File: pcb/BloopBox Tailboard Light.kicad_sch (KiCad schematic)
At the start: 18 parts, among them J1 USB_C_Receptacle_Power, J2 Barrel_Jack, J3 Mainboard, SW1 Button1, SW2 Button2, U1 HT7533-1

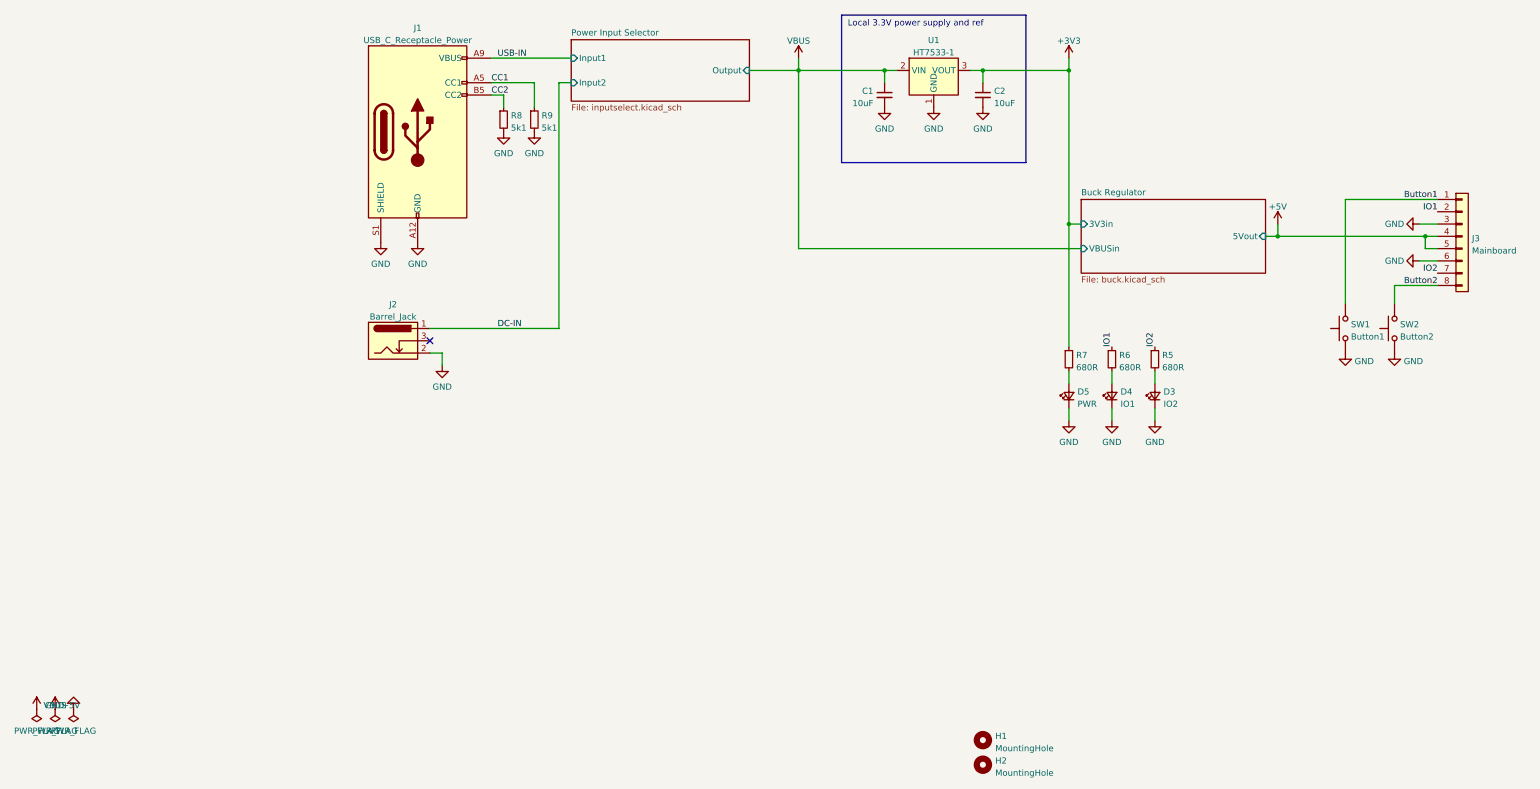
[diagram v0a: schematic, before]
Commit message: feat: remove active circuitry from schematics
Removing all active circuitry from the light-version of the Tailboard
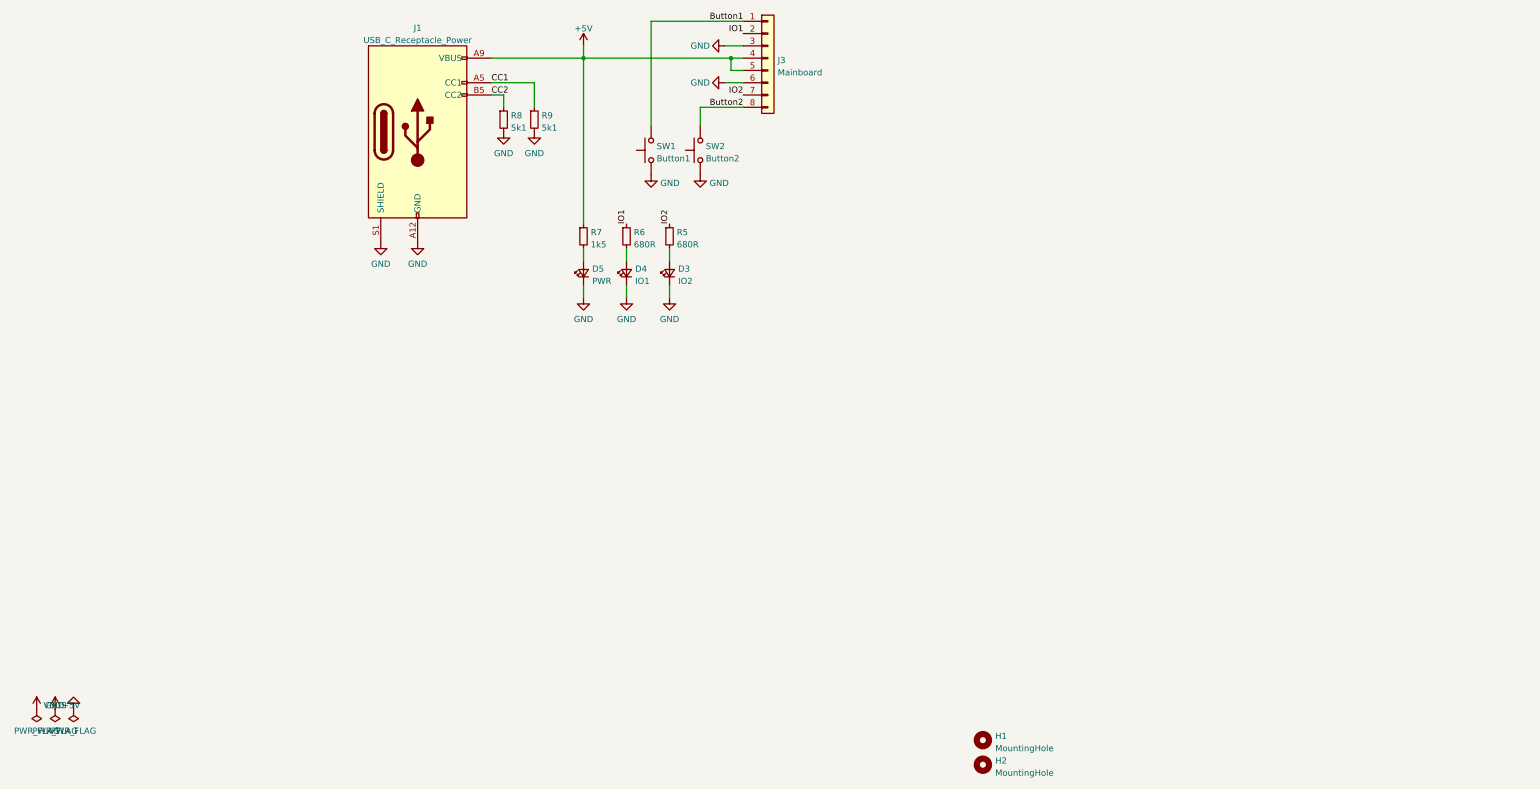
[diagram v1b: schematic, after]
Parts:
- removed C1: 10uF, Capacitor_SMD:C_0805_2012Metric, symbol Device:C_Small
- removed C2: 10uF, Capacitor_SMD:C_0402_1005Metric, symbol Device:C_Small
- removed J2: Barrel_Jack, Connector_BarrelJack:BarrelJack_Horizontal, symbol Connector:Barrel_Jack_Switch
- removed U1: HT7533-1, Package_TO_SOT_SMD:SOT-89-3, symbol Regulator_Linear:HT75xx-1-SOT89
- R7: value 680R -> 1k5
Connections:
- net +3V3 is gone; now on net +5V: R7.1
- net USB-IN is gone; now on net +5V: J1.A9 (VBUS), J1.B9 (VBUS)
- no-connect marks 1 -> 0
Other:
- removed sheet Buck Regulator
- removed sheet Power Input Selector
- note removed: "Local 3.3V power supply and ref"
- moved on the sheet: D3, D4, D5, J3, R5, R6, R7, SW1, SW2

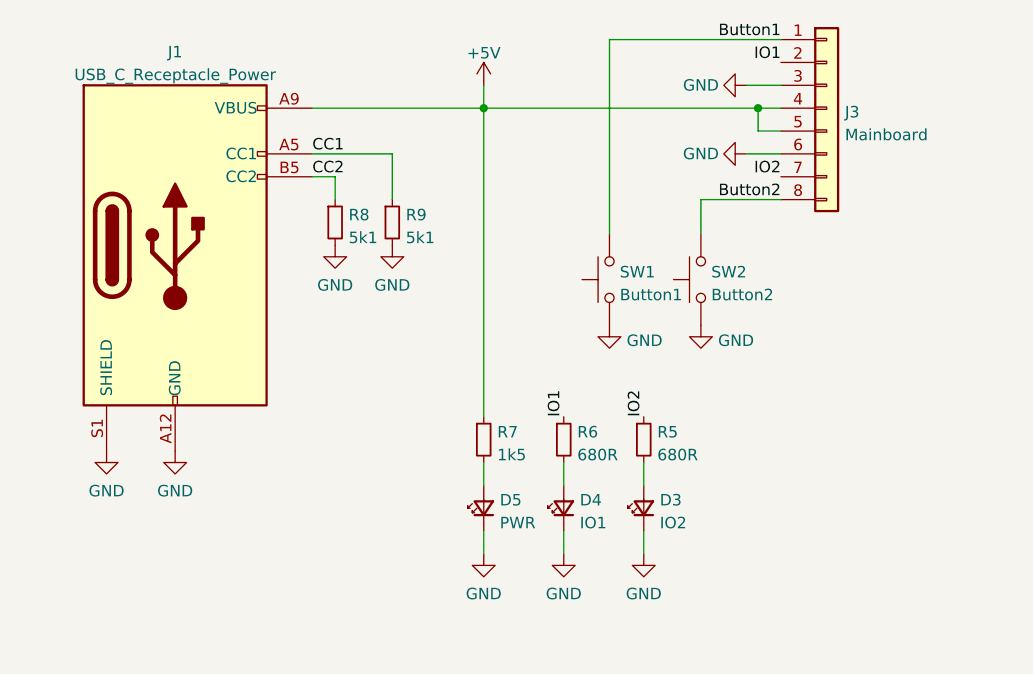
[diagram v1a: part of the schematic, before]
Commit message: feat: remove active circuitry from PCB
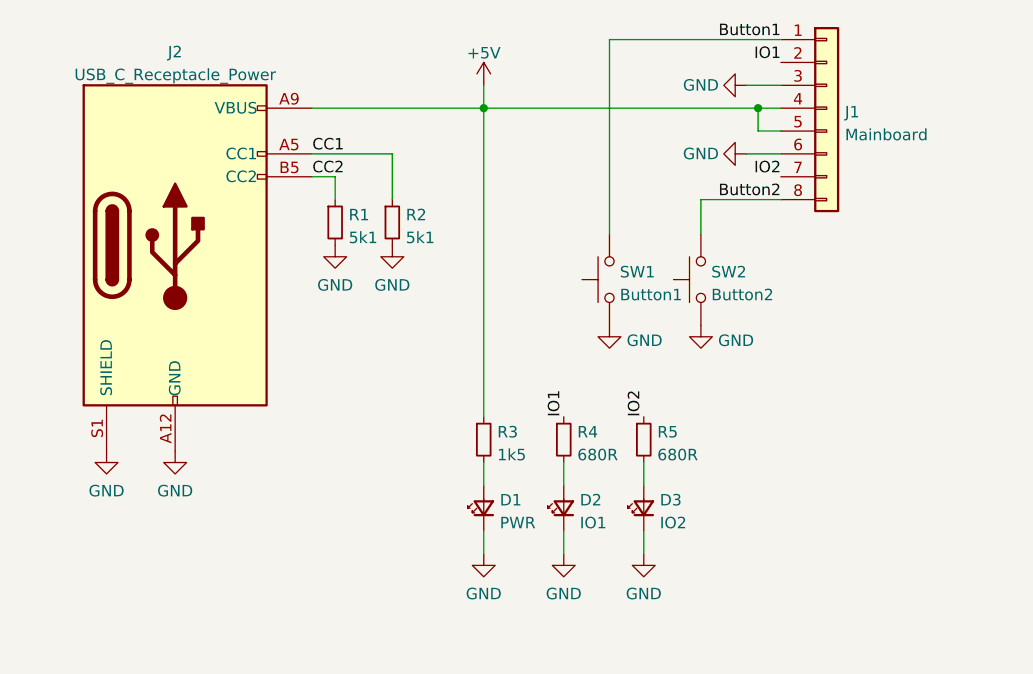
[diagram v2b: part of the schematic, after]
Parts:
- renumbered D5 to D1, D4 to D2, J3 to J1, J1 to J2, R8 to R1, R9 to R2, R7 to R3, R6 to R4

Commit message: fix: change resistors to 0603 footptint
Changing the resistor footprints to 0603 to make hand-soldering easier, since this board does not have the size restraints of the full version of the Tailboard
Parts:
- R1, R2: footprint Resistor_SMD:R_0402_1005Metric -> Resistor_SMD:R_0603_1608Metric; LCSC C25905 -> C23186
- R3: footprint Resistor_SMD:R_0402_1005Metric -> Resistor_SMD:R_0603_1608Metric; LCSC C25130 -> C22843
- R4, R5: footprint Resistor_SMD:R_0402_1005Metric -> Resistor_SMD:R_0603_1608Metric; LCSC C25130 -> C23228
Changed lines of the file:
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@@
       (effects (font (size 1.27 1.27)) (justify left))
     )
-    (property "Footprint" "Resistor_SMD:R_0402_1005Metric" (id 2) (at 93.98 83.82 0)
+    (property "Footprint" "Resistor_SMD:R_0603_1608Metric" (id 2) (at 93.98 83.82 0)
       (effects (font (size 1.27 1.27)) hide)
     )
@@
       (effects (font (size 1.27 1.27)) hide)
     )
-    (property "LCSC" "C25130" (id 4) (at 93.98 83.82 0)
+    (property "LCSC" "C23228" (id 4) (at 93.98 83.82 0)
       (effects (font (size 1.27 1.27)) hide)
     )
@@
       (effects (font (size 1.27 1.27)) (justify left))
     )
-    (property "Footprint" "Resistor_SMD:R_0402_1005Metric" (id 2) (at 59.69 59.69 0)
+    (property "Footprint" "Resistor_SMD:R_0603_1608Metric" (id 2) (at 59.69 59.69 0)
       (effects (font (size 1.27 1.27)) hide)
     )
@@
       (effects (font (size 1.27 1.27)) hide)
     )
-    (property "LCSC" "C25905" (id 4) (at 59.69 59.69 0)
+    (property "LCSC" "C23186" (id 4) (at 59.69 59.69 0)
       (effects (font (size 1.27 1.27)) hide)
     )
@@
       (effects (font (size 1.27 1.27)) (justify left))
     )
-    (property "Footprint" "Resistor_SMD:R_0402_1005Metric" (id 2) (at 76.2 83.82 0)
+    (property "Footprint" "Resistor_SMD:R_0603_1608Metric" (id 2) (at 76.2 83.82 0)
       (effects (font (size 1.27 1.27)) hide)
     )
@@
       (effects (font (size 1.27 1.27)) hide)
     )
-    (property "LCSC" "C25130" (id 4) (at 76.2 83.82 0)
+    (property "LCSC" "C22843" (id 4) (at 76.2 83.82 0)
       (effects (font (size 1.27 1.27)) hide)
     )
@@
       (effects (font (size 1.27 1.27)) (justify left))
     )
-    (property "Footprint" "Resistor_SMD:R_0402_1005Metric" (id 2) (at 85.09 83.82 0)
+    (property "Footprint" "Resistor_SMD:R_0603_1608Metric" (id 2) (at 85.09 83.82 0)
       (effects (font (size 1.27 1.27)) hide)
     )
@@
       (effects (font (size 1.27 1.27)) hide)
     )
-    (property "LCSC" "C25130" (id 4) (at 85.09 83.82 0)
+    (property "LCSC" "C23228" (id 4) (at 85.09 83.82 0)
       (effects (font (size 1.27 1.27)) hide)
     )
@@
       (effects (font (size 1.27 1.27)) (justify left))
     )
-    (property "Footprint" "Resistor_SMD:R_0402_1005Metric" (id 2) (at 66.04 59.69 0)
+    (property "Footprint" "Resistor_SMD:R_0603_1608Metric" (id 2) (at 66.04 59.69 0)
       (effects (font (size 1.27 1.27)) hide)
     )
@@
       (effects (font (size 1.27 1.27)) hide)
     )
-    (property "LCSC" "C25905" (id 4) (at 66.04 59.69 0)
+    (property "LCSC" "C23186" (id 4) (at 66.04 59.69 0)
       (effects (font (size 1.27 1.27)) hide)
     )
@@
     )
     (path "/931250ab-da92-4d69-a65a-c6a6eb03f196"
-      (reference "R1") (unit 1) (value "5k1") (footprint "Resistor_SMD:R_0402_1005Metric")
+      (reference "R1") (unit 1) (value "5k1") (footprint "Resistor_SMD:R_0603_1608Metric")
     )
     (path "/ed80fbb0-747a-4dc0-9051-2fa7315a49b6"
-      (reference "R2") (unit 1) (value "5k1") (footprint "Resistor_SMD:R_0402_1005Metric")
+      (reference "R2") (unit 1) (value "5k1") (footprint "Resistor_SMD:R_0603_1608Metric")
     )
     (path "/baf7203f-1602-4c1d-bb1f-97a9cf43a038"
-      (reference "R3") (unit 1) (value "1k5") (footprint "Resistor_SMD:R_0402_1005Metric")
+      (reference "R3") (unit 1) (value "1k5") (footprint "Resistor_SMD:R_0603_1608Metric")
     )
     (path "/da8d367e-8024-4e7f-ad67-2ae57bfa11f6"
-      (reference "R4") (unit 1) (value "680R") (footprint "Resistor_SMD:R_0402_1005Metric")
+      (reference "R4") (unit 1) (value "680R") (footprint "Resistor_SMD:R_0603_1608Metric")
     )
     (path "/597a46d4-75b0-423b-9306-f50224336f6c"
-      (reference "R5") (unit 1) (value "680R") (footprint "Resistor_SMD:R_0402_1005Metric")
+      (reference "R5") (unit 1) (value "680R") (footprint "Resistor_SMD:R_0603_1608Metric")
     )
     (path "/23e9fb92-8832-487e-8c7c-90b66b9656b3"
